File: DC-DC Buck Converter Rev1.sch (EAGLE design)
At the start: 37 parts, among them J1 APP_2POS_CONFIG5V_HORIZ, J2 APP_2POS_CONFIG5V_HORIZ, J4 APP_2POS_CONFIG12V_HORIZ, U1 OKI-78SR-5/1.5-W36HC

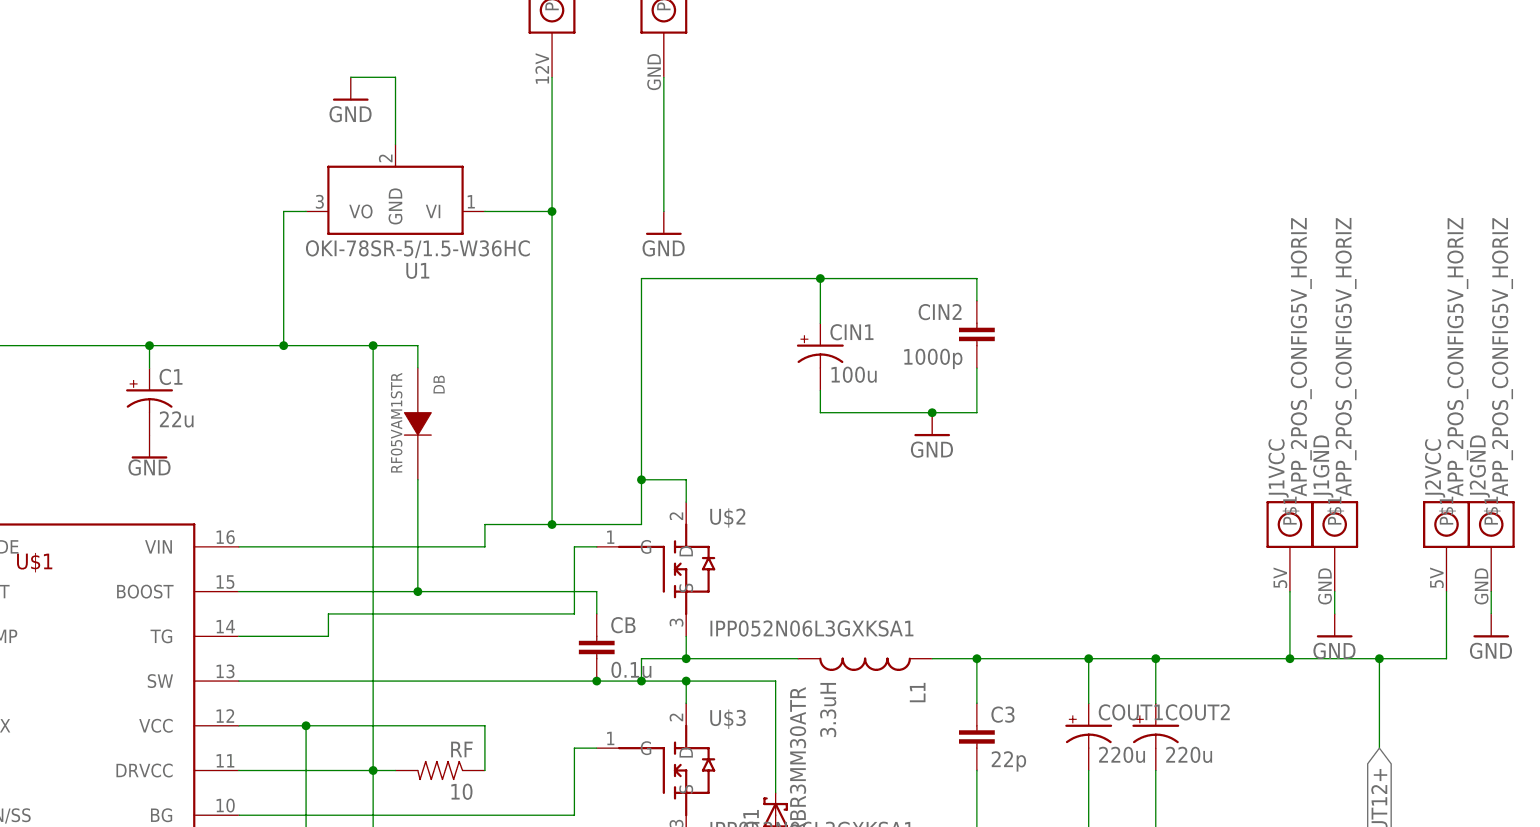
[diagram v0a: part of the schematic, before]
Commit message: Small changes
Replaced Oki capacitor, moved diode, deleted output anderson
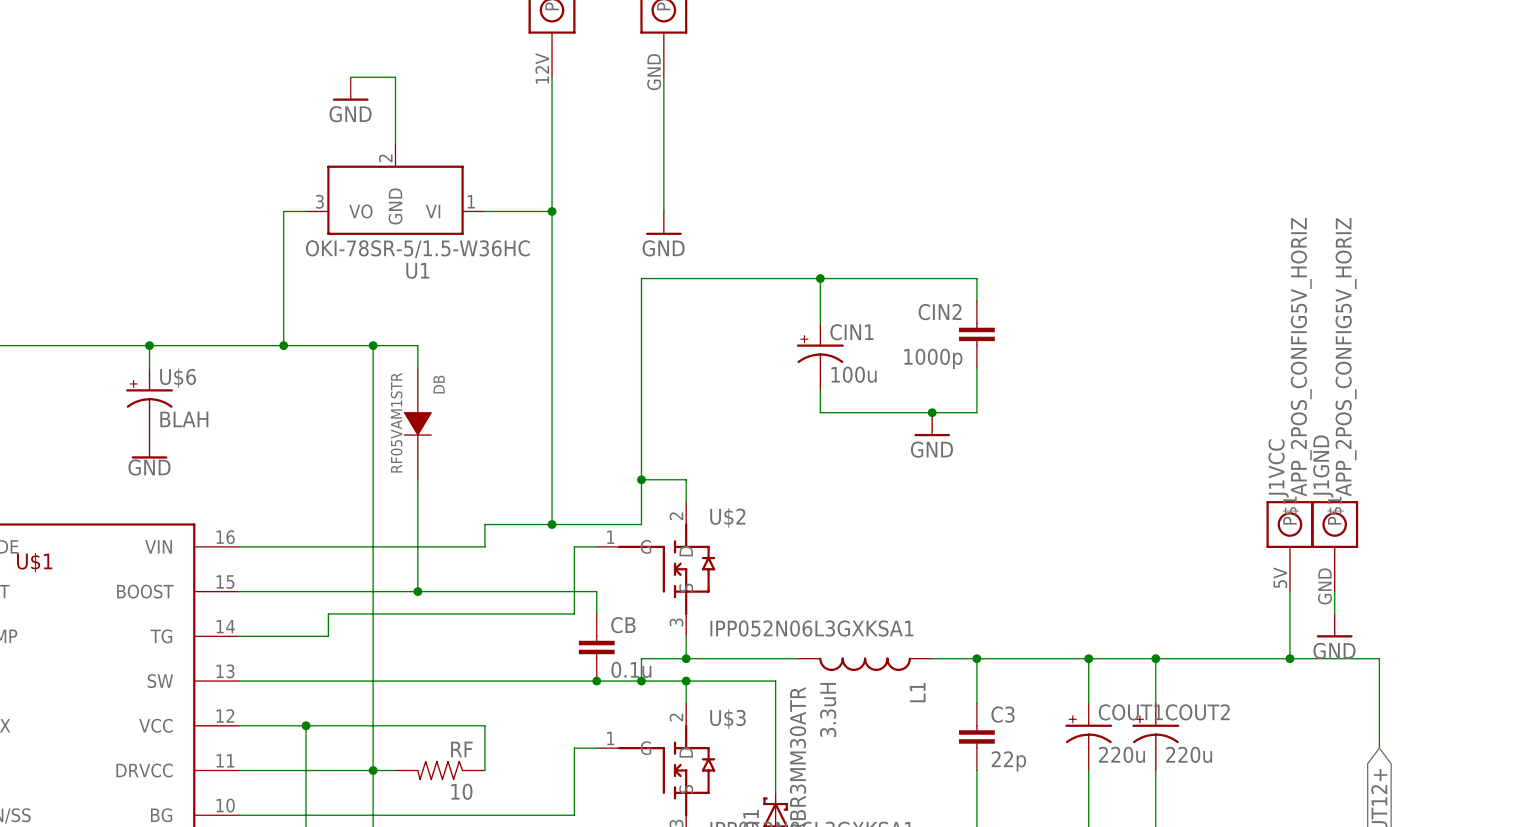
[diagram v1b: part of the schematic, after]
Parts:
- removed C1: 22u, buckconverter:UCZ1K220MCL1GS
- removed J2: APP_2POS_CONFIG5V_HORIZ, MRDT-Connectors:APP_2POS_CONFIG5V_HORIZ
- added U$6: BLAH, buckconverter:BLAH
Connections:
- net 5V: now also U$6.+; no longer C1.+
- net GND: now also U$6.-; no longer C1.-, J2GND.P$1
- net VOUT12+: no longer J2VCC.P$1
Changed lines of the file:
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@@
 <?xml version="1.0" encoding="utf-8"?>
 <!DOCTYPE eagle SYSTEM "eagle.dtd">
-<eagle version="8.4.0">
+<eagle version="8.4.1">
 <drawing>
 <settings>
@@
 <part name="GND5" library="SparkFun-Aesthetics" library_urn="urn:adsk.eagle:library:507" deviceset="GND" device=""/>
 <part name="J1" library="MRDT-Connectors" deviceset="APP_2POS_CONFIG" device="5V_HORIZ"/>
-<part name="J2" library="MRDT-Connectors" deviceset="APP_2POS_CONFIG" device="5V_HORIZ"/>
-<part name="C1" library="buckconverter" deviceset="UCZ1K220MCL1GS" device="" value="22u"/>
 <part name="GND2" library="SparkFun-PowerSymbols" library_urn="urn:adsk.eagle:library:530" deviceset="GND" device=""/>
 <part name="L1" library="buckconverter" deviceset="PQ3218-3R3-70-T" device="" value="3.3uH"/>
@@
 <part name="GND8" library="SparkFun-Aesthetics" library_urn="urn:adsk.eagle:library:507" deviceset="GND" device=""/>
 <part name="GND9" library="SparkFun-Aesthetics" library_urn="urn:adsk.eagle:library:507" deviceset="GND" device=""/>
-<part name="GND10" library="SparkFun-Aesthetics" library_urn="urn:adsk.eagle:library:507" deviceset="GND" device=""/>
 <part name="H1" library="MRDT-Hardware" deviceset="MOUNTING_HOLE" device="#8"/>
 <part name="H2" library="MRDT-Hardware" deviceset="MOUNTING_HOLE" device="#8"/>
@@
 <part name="U$4" library="buckconverter" deviceset="530002B02500G" device=""/>
 <part name="U$5" library="buckconverter" deviceset="530002B02500G" device=""/>
+<part name="U$6" library="buckconverter" deviceset="BLAH" device=""/>
 </parts>
 <sheets>
@@
 <instance part="J1" gate="GND" x="228.6" y="137.16" rot="R90"/>
 <instance part="J1" gate="VCC" x="223.52" y="137.16" rot="R90"/>
-<instance part="J2" gate="GND" x="246.38" y="137.16" rot="R90"/>
-<instance part="J2" gate="VCC" x="241.3" y="137.16" rot="R90"/>
-<instance part="C1" gate="G$1" x="93.98" y="149.86"/>
 <instance part="GND2" gate="1" x="93.98" y="144.78"/>
 <instance part="L1" gate="G$1" x="175.26" y="121.92" rot="R270"/>
@@
 <instance part="GND8" gate="1" x="160.02" y="93.98"/>
 <instance part="GND9" gate="1" x="228.6" y="124.46"/>
-<instance part="GND10" gate="1" x="246.38" y="124.46"/>
 <instance part="H1" gate="G$1" x="-40.64" y="236.22"/>
 <instance part="H2" gate="G$1" x="-40.64" y="228.6"/>
@@
 <instance part="U$4" gate="G$1" x="58.42" y="200.66"/>
 <instance part="U$5" gate="G$1" x="81.28" y="200.66"/>
+<instance part="U$6" gate="G$1" x="93.98" y="149.86"/>
 </instances>
 <busses>
@@
 </segment>
 <segment>
-<pinref part="C1" gate="G$1" pin="-"/>
-<pinref part="GND2" gate="1" pin="GND"/>
-</segment>
-<segment>
 <pinref part="C3" gate="G$1" pin="2"/>
 <pinref part="COUT2" gate="G$1" pin="-"/>
@@
 </segment>
 <segment>
-<pinref part="GND10" gate="1" pin="GND"/>
-<pinref part="J2" gate="GND" pin="P$1"/>
-<wire x1="246.38" y1="127" x2="246.38" y2="129.54" width="0.1524" layer="91"/>
-</segment>
-<segment>
 <pinref part="GND5" gate="1" pin="GND"/>
 <pinref part="U1" gate="G$1" pin="GND"/>
 <wire x1="116.84" y1="187.96" x2="121.92" y2="187.96" width="0.1524" layer="91"/>
 <wire x1="121.92" y1="187.96" x2="121.92" y2="180.34" width="0.1524" layer="91"/>
+</segment>
+<segment>
+<pinref part="GND2" gate="1" pin="GND"/>
+<pinref part="U$6" gate="G$1" pin="-"/>
 </segment>
 </net>
@@
 <wire x1="109.22" y1="157.48" x2="119.38" y2="157.48" width="0.1524" layer="91"/>
 <wire x1="119.38" y1="157.48" x2="124.46" y2="157.48" width="0.1524" layer="91"/>
-<pinref part="C1" gate="G$1" pin="+"/>
 <wire x1="93.98" y1="157.48" x2="93.98" y2="154.94" width="0.1524" layer="91"/>
 <pinref part="DB" gate="G$1" pin="A"/>
@@
 <wire x1="109.22" y1="172.72" x2="109.22" y2="157.48" width="0.1524" layer="91"/>
 <junction x="109.22" y="157.48"/>
+<pinref part="U$6" gate="G$1" pin="+"/>
 </segment>
 </net>
@@
 <wire x1="223.52" y1="129.54" x2="223.52" y2="121.92" width="0.1524" layer="91"/>
 <wire x1="223.52" y1="121.92" x2="208.28" y2="121.92" width="0.1524" layer="91"/>
-<pinref part="J2" gate="VCC" pin="P$1"/>
-<wire x1="241.3" y1="129.54" x2="241.3" y2="121.92" width="0.1524" layer="91"/>
-<wire x1="241.3" y1="121.92" x2="233.68" y2="121.92" width="0.1524" layer="91"/>
 <junction x="223.52" y="121.92"/>
 <label x="233.68" y="111.76" size="1.778" layer="95" rot="R270" xref="yes"/>
 <wire x1="233.68" y1="121.92" x2="223.52" y2="121.92" width="0.1524" layer="91"/>
 <wire x1="233.68" y1="111.76" x2="233.68" y2="121.92" width="0.1524" layer="91"/>
-<junction x="233.68" y="121.92"/>
 <pinref part="L1" gate="G$1" pin="1"/>
 <wire x1="182.88" y1="121.92" x2="187.96" y2="121.92" width="0.1524" layer="91"/>
